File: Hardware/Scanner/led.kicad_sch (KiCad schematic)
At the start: 20 parts, among them U5 TLC59208FIPWR

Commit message: added footprint for MTSM2601SMF1-100
Signed-off-by: lokimetasmith <lokimail@gmail.com>
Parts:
- removed C18: 100nF, Capacitor_SMD:C_0603_1608Metric_Pad1.08x0.95mm_HandSolder, symbol Device:C
- removed D10: 1650nm, LED_SMD:LED_1206_3216Metric_Pad1.42x1.75mm_HandSolder, symbol Device:LED
- removed D11: 1720nm, LED_SMD:LED_1206_3216Metric_Pad1.42x1.75mm_HandSolder, symbol Device:LED
- removed D4: 855nm, LED_SMD:LED_1206_3216Metric_Pad1.42x1.75mm_HandSolder, symbol Device:LED
- removed D5: 940nm, LED_SMD:LED_1206_3216Metric_Pad1.42x1.75mm_HandSolder, symbol Device:LED
- removed D6: 1050nm, LED_SMD:LED_1206_3216Metric_Pad1.42x1.75mm_HandSolder, symbol Device:LED
- removed D7: 1300nm, LED_SMD:LED_1206_3216Metric_Pad1.42x1.75mm_HandSolder, symbol Device:LED
- removed D8: 1460nm, LED_SMD:LED_1206_3216Metric_Pad1.42x1.75mm_HandSolder, symbol Device:LED
- removed D9: 1550nm, LED_SMD:LED_1206_3216Metric_Pad1.42x1.75mm_HandSolder, symbol Device:LED
- removed R24: 1k, Resistor_SMD:R_0603_1608Metric_Pad0.98x0.95mm_HandSolder, symbol Device:R
- removed R25: 56, Resistor_SMD:R_0603_1608Metric_Pad0.98x0.95mm_HandSolder, symbol Device:R
- removed R26, R29, R30: 150, Resistor_SMD:R_0603_1608Metric_Pad0.98x0.95mm_HandSolder, symbol Device:R
- removed R27, R28: 240, Resistor_SMD:R_0603_1608Metric_Pad0.98x0.95mm_HandSolder, symbol Device:R
- removed R31: 40, Resistor_SMD:R_0603_1608Metric_Pad0.98x0.95mm_HandSolder, symbol Device:R
- removed R32: 130, Resistor_SMD:R_0603_1608Metric_Pad0.98x0.95mm_HandSolder, symbol Device:R
- removed TP3: Test_3.3V, TestPoint:TestPoint_Pad_D1.5mm, symbol Connector:TestPoint
- removed U5: TLC59208FIPWR, TLC59208FIPWR:SOP65P640X120-16N, symbol TLC59208:TLC59208FIPWR
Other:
- note removed: "855nm RS 173-6298 940nm RS 173-6348 1050nm digikey 11251359 nd 1200nm digikey 1125-1356-nd 1300nm digikey 1125-1335-nd 1450nm digikey 1125-1360-nd 1550nm digikey 1125-mtsm5015-194-irt-nd 1650nm digikey 1125-1362-nd"
- company: Plastic Scanner -> (none)
- title: Development Board -> (none)

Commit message: lots of changes, added footprints, fixed broken schemaitcs, fixed kicad 7.0 issues
Signed-off-by: lokimetasmith <lokimail@gmail.com>
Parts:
- added C18: 100nF, Capacitor_SMD:C_0603_1608Metric_Pad1.08x0.95mm_HandSolder, symbol Device:C
- added D10: 1650nm, LED_SMD:LED_1206_3216Metric_Pad1.42x1.75mm_HandSolder, symbol Device:LED
- added D11: 1720nm, LED_SMD:LED_1206_3216Metric_Pad1.42x1.75mm_HandSolder, symbol Device:LED
- added D4: 855nm, LED_SMD:LED_1206_3216Metric_Pad1.42x1.75mm_HandSolder, symbol Device:LED
- added D5: 940nm, LED_SMD:LED_1206_3216Metric_Pad1.42x1.75mm_HandSolder, symbol Device:LED
- added D6: 1050nm, LED_SMD:LED_1206_3216Metric_Pad1.42x1.75mm_HandSolder, symbol Device:LED
- added D7: 1300nm, LED_SMD:LED_1206_3216Metric_Pad1.42x1.75mm_HandSolder, symbol Device:LED
- added D8: 1460nm, LED_SMD:LED_1206_3216Metric_Pad1.42x1.75mm_HandSolder, symbol Device:LED
- added D9: 1550nm, LED_SMD:LED_1206_3216Metric_Pad1.42x1.75mm_HandSolder, symbol Device:LED
- added R24: 1k, Resistor_SMD:R_0603_1608Metric_Pad0.98x0.95mm_HandSolder, symbol Device:R
- added R25: 56, Resistor_SMD:R_0603_1608Metric_Pad0.98x0.95mm_HandSolder, symbol Device:R
- added R26, R29, R30: 150, Resistor_SMD:R_0603_1608Metric_Pad0.98x0.95mm_HandSolder, symbol Device:R
- added R27, R28: 240, Resistor_SMD:R_0603_1608Metric_Pad0.98x0.95mm_HandSolder, symbol Device:R
- added R31: 40, Resistor_SMD:R_0603_1608Metric_Pad0.98x0.95mm_HandSolder, symbol Device:R
- added R32: 130, Resistor_SMD:R_0603_1608Metric_Pad0.98x0.95mm_HandSolder, symbol Device:R
- added TP3: Test_3.3V, TestPoint:TestPoint_Pad_D1.5mm, symbol Connector:TestPoint
- added U5: TLC59208FIPWR, TLC59208FIPWR:SOP65P640X120-16N, symbol TLC59208:TLC59208FIPWR
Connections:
- new net: D8.1 (K), R29.2
- new net: R32.1, U5.12 (~{OUT7})
- new net: D11.1 (K), R32.2
- new net: R30.1, U5.10 (~{OUT5})
- new net: R31.1, U5.11 (~{OUT6})
- new net: R25.1, U5.4 (~{OUT0})
- new net: R26.1, U5.5 (~{OUT1})
- new net: R27.1, U5.6 (~{OUT2})
- new net: R28.1, U5.7 (~{OUT3})
- new net: R29.1, U5.9 (~{OUT4})
- new net: D5.1 (K), R26.2
- new net: D9.1 (K), R30.2
- new net: D4.1 (K), R25.2
- new net: D7.1 (K), R28.2
- new net: D6.1 (K), R27.2
- new net: D10.1 (K), R31.2
- new net +3.3V: C18.1, D10.2 (A), D11.2 (A), D4.2 (A), D5.2 (A), D6.2 (A), D7.2 (A), D8.2 (A), D9.2 (A), R24.2, TP3.1, U5.16 (VCC)
- new net GND: C18.2, U5.1 (A0), U5.2 (A1), U5.3 (A2), U5.8 (GND)
- new net LED_RESET: R24.1, U5.13 (~{RESET})
- new net SCL: U5.14 (SCL)
- new net SDA: U5.15 (SDA)
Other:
- note added: "855nm RS 173-6298 940nm RS 173-6348 1050nm digikey 11251359 nd 1200nm digikey 1125-1356-nd 1300nm digikey 1125-1335-nd 1450nm digikey 1125-1360-nd 1550nm digikey 1125-mtsm5015-194-irt-nd 1650nm digikey 1125-1362-nd"
- note added: "Optimal values. Grouping is 10% +/- and not likely to work, spread is 35nm, and so need 5nm per step to have a four bit differentiation Spectral FWHM (Full Width at Half Maximum) needs to be 5nm 1180nm 1200nm 1215nm Grouping is 10% +/- and not likely to work 1680nm 1700nm 1720nm 1740nm"
- company: (none) -> Plastic Scanner
- title: (none) -> Development Board

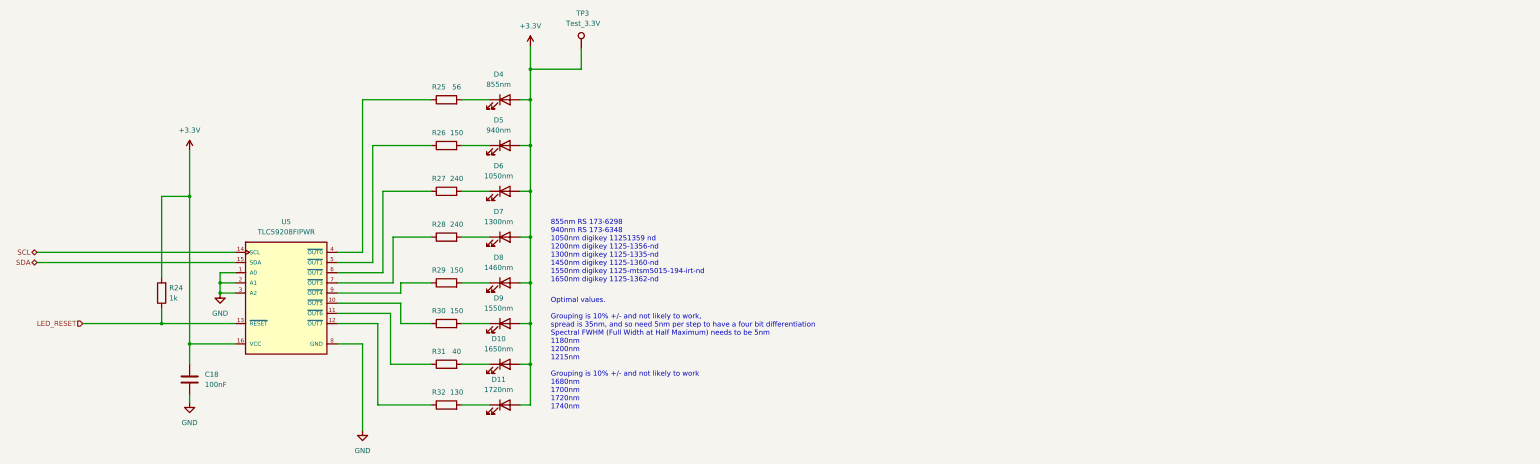
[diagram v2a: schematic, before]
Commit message: updated schematic, and layout, updated bom, fully converted to 3.3v for Voltage input only
Signed-off-by: lokimetasmith <lokimail@gmail.com>
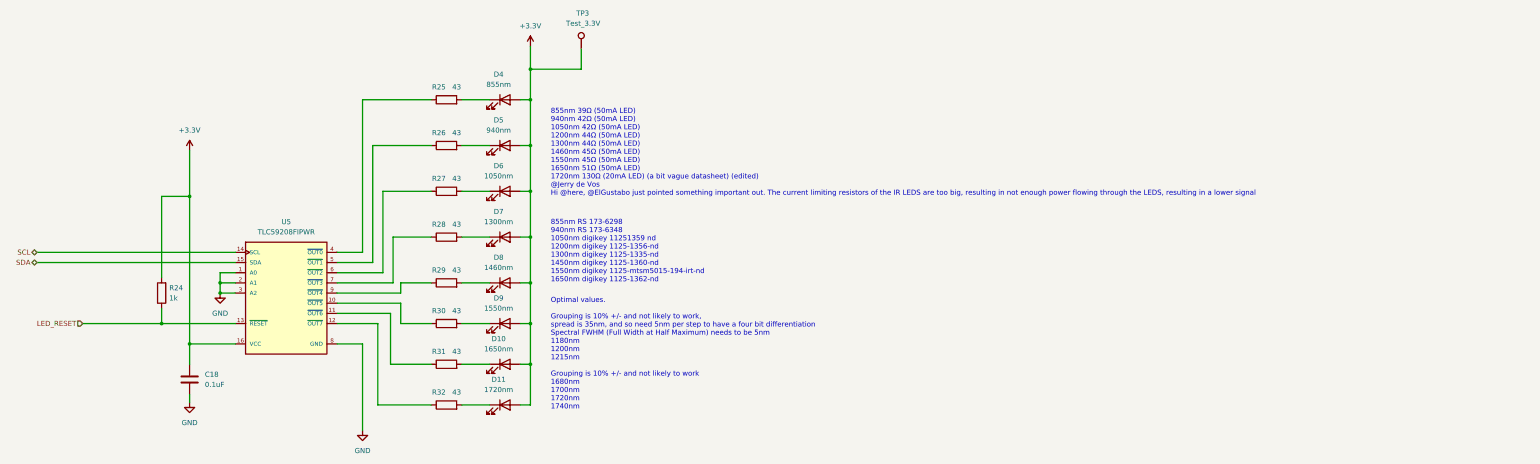
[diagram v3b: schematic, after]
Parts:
- C18: value 100nF -> 0.1uF; digikey description (none) -> CAP CER 0.1UF 16V X7R 0603; digikey part number (none) -> 311-1088-1-ND
- D10: digikey description (none) -> SWIR EMITTER 1650NM 1206 SMD MTSM5016-199-IR; digikey part number (none) -> 1125-1354-ND
- D11: digikey description (none) -> SWIR EMITTER 1200NM 1206 SMD; digikey part number (none) -> 1125-MTSM0012-194-IRCT-ND
- D4: digikey description (none) -> LED CHIP IR WLP 850NM 1206 SMD; digikey part number (none) -> 1516-1269-1-ND
- D5: digikey description (none) -> EMITTER IR 940NM 65MA 1206; digikey part number (none) -> 1080-1350-1-ND
- D6: digikey description (none) -> SWIR EMITTER 1050NM 1206 SMD; digikey part number (none) -> 1125-1342-ND
- D7: digikey description (none) -> SWIR EMITTER 1300NM 1206 SMD FLA; digikey part number (none) -> 5242-OIS-1501300N-X-TCT-ND
- D8: digikey description (none) -> SWIR EMITTER 1460NM 1206 SMD; digikey part number (none) -> 1125-MTSM6014-194-IRCT-ND
- D9: digikey description (none) -> SWIR EMITTER 1550NM 1206 SMD FLA; digikey part number (none) -> 5242-OIS-1501550N-X-TCT-ND
- R24: digikey description (none) -> RES 1K OHM 1% 1/10W 0603; digikey part number (none) -> 311-1.00KHRCT-ND
- R25: value 56 -> 43; digikey description (none) -> RES SMD 43 OHM 5% 1/3W 0603; digikey part number (none) -> P43.00BZCT-ND
- R26, R29, R30: value 150 -> 43; digikey description (none) -> RES SMD 43 OHM 5% 1/3W 0603; digikey part number (none) -> P43.00BZCT-ND
- R27, R28: value 240 -> 43; digikey description (none) -> RES SMD 43 OHM 5% 1/3W 0603; digikey part number (none) -> P43.00BZCT-ND
- R31: value 40 -> 43; digikey description (none) -> RES SMD 43 OHM 5% 1/3W 0603; digikey part number (none) -> P43.00BZCT-ND
- R32: value 130 -> 43; digikey description (none) -> RES SMD 43 OHM 5% 1/3W 0603; digikey part number (none) -> P43.00BZCT-ND; mouser description (none) -> ERJ-3EKF1300V; mouser part number (none) -> 667-ERJ-3EKF1300V
- U5: digikey description (none) -> TLC59208FIPWR; digikey part number (none) -> 296-36508-2-ND
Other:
- note added: "855nm 39Ω (50mA LED) 940nm 42Ω (50mA LED) 1050nm 42Ω (50mA LED) 1200nm 44Ω (50mA LED) 1300nm 44Ω (50mA LED) 1460nm 45Ω (50mA LED) 1550nm 45Ω (50mA LED) 1650nm 51Ω (50mA LED) 1720nm 130Ω (20mA LED) (a bit vague datasheet) (edited) @Jerry de Vos Hi @here, @ElGustabo just pointed something important out. The current limiting resistors of the IR LEDS are too big, resulting in not enough power flowing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"
